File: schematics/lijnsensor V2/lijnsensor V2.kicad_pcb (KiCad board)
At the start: 2 copper layers, 137 x 105 mm, 30 parts, among them J1 Conn_01x04_Pin, U1 USBLC6-2SC6, U10 AS7343xDLG, U11 AS7343xDLG, U2 TCA9548APWR, U3 TLV75718PDBV, U4 AS7343xDLG, U5 AS7343xDLG, U6 AS7343xDLG, U7 AS7343xDLG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

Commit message: update de schematics
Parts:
- added R17: 10K, Resistor_SMD:R_0603_1608Metric, F.Cu at (124.2, 56.4)
- moved C1 3.33 mm to (121.2, 66.8)
- moved C2 2.41 mm to (128.4, 66.1)
- moved U3 1.91 mm to (125.1, 65.8)
- moved U2 1.74 mm to (118.0, 58.4), turned to 180 degrees
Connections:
- U2 pad 3: unconnected-(U2-~{RESET}-Pad3) -> Net-(U2-~{RESET})
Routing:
- net +1V8: track 255.5 -> 0.00 mm
- net Net-(U2-SC3): track 124.9 -> 0.00 mm, vias 8 -> 0
- net Net-(U2-SD3): track 124.5 -> 0.00 mm, vias 6 -> 0
- net Net-(U11-SCL): track 117.5 -> 0.00 mm, vias 4 -> 0
- net Net-(U11-SDA): track 112.7 -> 0.00 mm
- net Net-(U2-SC2): track 92.4 -> 0.00 mm, vias 6 -> 0
- net Net-(U2-SD2): track 91.5 -> 0.00 mm, vias 4 -> 0
- net Net-(U10-SCL): track 87.1 -> 0.00 mm, vias 2 -> 0
- net Net-(U10-SDA): track 82.4 -> 0.00 mm
- net Net-(U2-SD1): track 63.2 -> 0.00 mm
- net Net-(U2-SC1): track 60.0 -> 0.00 mm, vias 4 -> 0
- net Net-(U2-SC5): track 53.8 -> 0.00 mm, vias 2 -> 0
- net Net-(U2-SD5): track 49.4 -> 0.00 mm
- net Net-(U2-SD0): track 22.0 -> 0.00 mm
- net Net-(U2-SC4): track 20.9 -> 0.00 mm
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- removed copper zone on F.Cu, net +3.3V

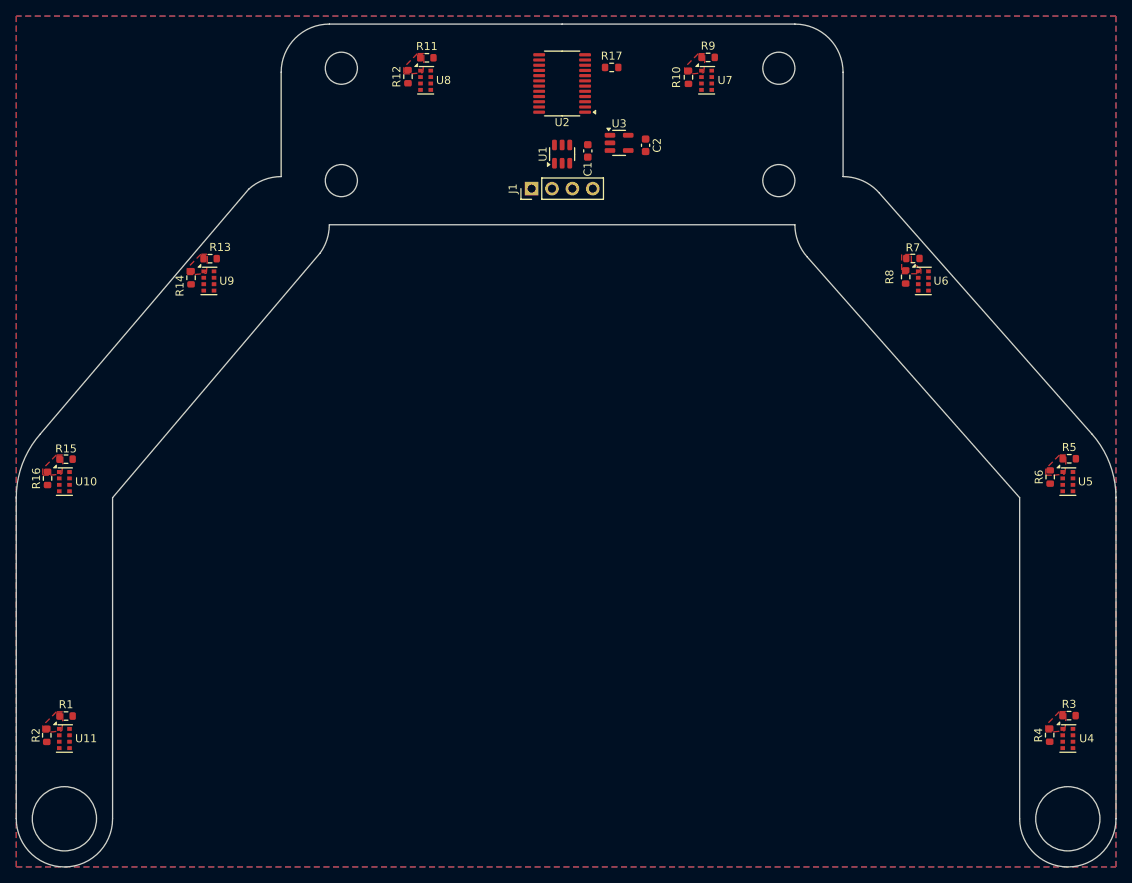
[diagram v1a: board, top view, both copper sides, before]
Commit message: teken al een deel van de lijnsensor
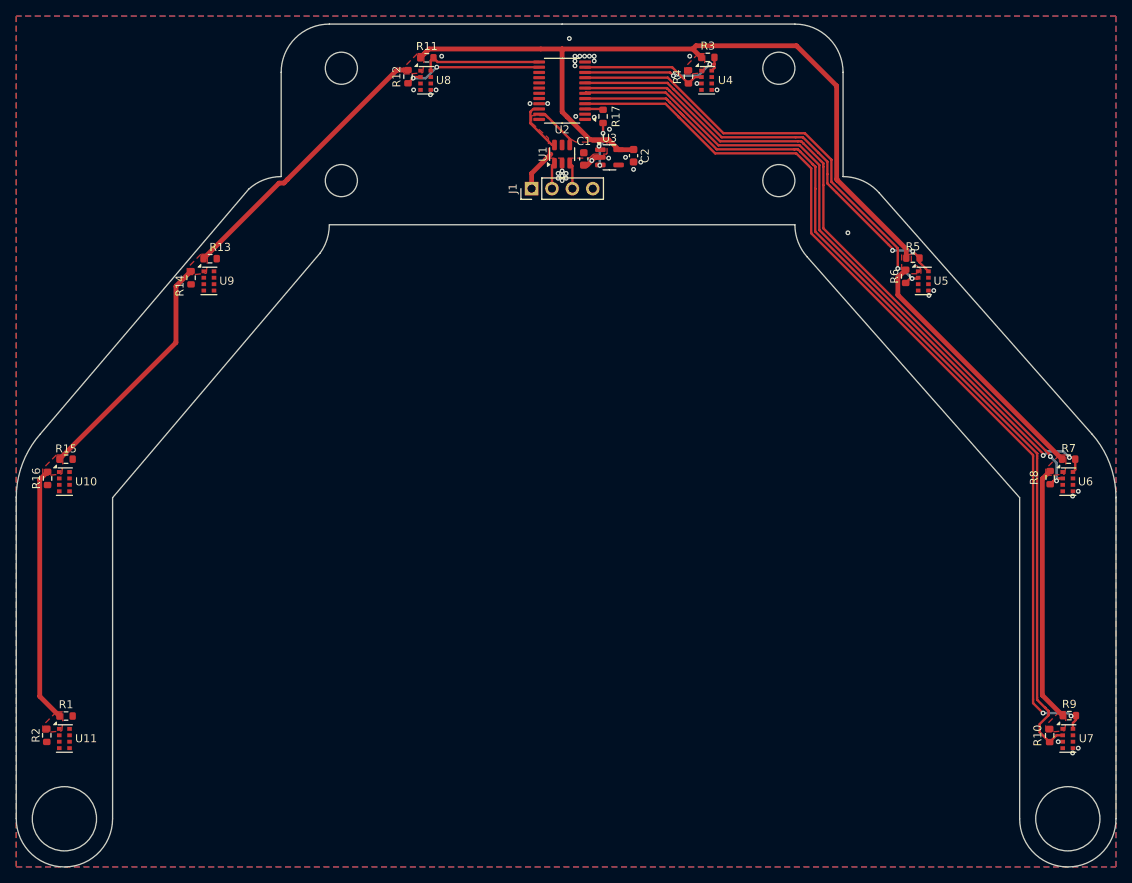
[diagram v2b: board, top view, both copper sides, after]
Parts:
- moved R10 93.5 mm to (178.7, 139.6)
- moved R3 93.5 mm to (136.2, 55.1)
- moved R9 93.5 mm to (181.2, 137.2)
- moved U4 93.5 mm to (136.0, 58.0)
- moved U7 93.5 mm to (181.0, 140.0)
- moved R4 93.5 mm to (133.7, 57.6)
- moved R5 31.7 mm to (161.7, 80.2)
- moved R7 31.6 mm to (181.1, 105.2)
- moved R6 30.8 mm to (160.8, 82.4)
- moved R8 30.8 mm to (178.8, 107.5)
- moved U5 30.8 mm to (163.0, 83.0)
- moved U6 30.8 mm to (181.0, 108.0)
- moved R17 6.19 mm to (123.1, 62.5), turned to 90 degrees
- moved U3 2.16 mm to (123.9, 67.6)
- moved C2 1.98 mm to (126.9, 67.4)
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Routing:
- net +1V8: track 0.00 -> 262.2 mm
- net Net-(U2-SC0): track 0.00 -> 118.9 mm
- net Net-(U2-SD0): track 0.00 -> 117.4 mm, vias 0 -> 2
- net Net-(U2-SD1): track 0.00 -> 87.1 mm, vias 0 -> 2
- net Net-(U2-SC1): track 0.00 -> 87.0 mm, vias 0 -> 2
- net Net-(U2-SC2): track 0.00 -> 56.0 mm, vias 0 -> 2
- net Net-(U2-SD2): track 0.00 -> 54.5 mm, vias 0 -> 2
- net Net-(U2-SD3): track 0.00 -> 18.7 mm, vias 0 -> 2
- net Net-(U2-SC4): track 0.00 -> 18.2 mm, vias 0 -> 2
- net Net-(U2-SC3): track 0.00 -> 15.7 mm
- net Net-(U2-SD4): track 0.00 -> 15.1 mm
- net +3.3V: track 0.00 -> 11.3 mm, vias 0 -> 3
- net /SCL: track 0.00 -> 6.79 mm
- net /SDA: track 0.00 -> 5.84 mm
- net Net-(J1-Pin_3): track 0.00 -> 3.30 mm
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- added copper zone on F.Cu, net +3.3V

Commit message: updata alle afmetingen en maak er een pdf van
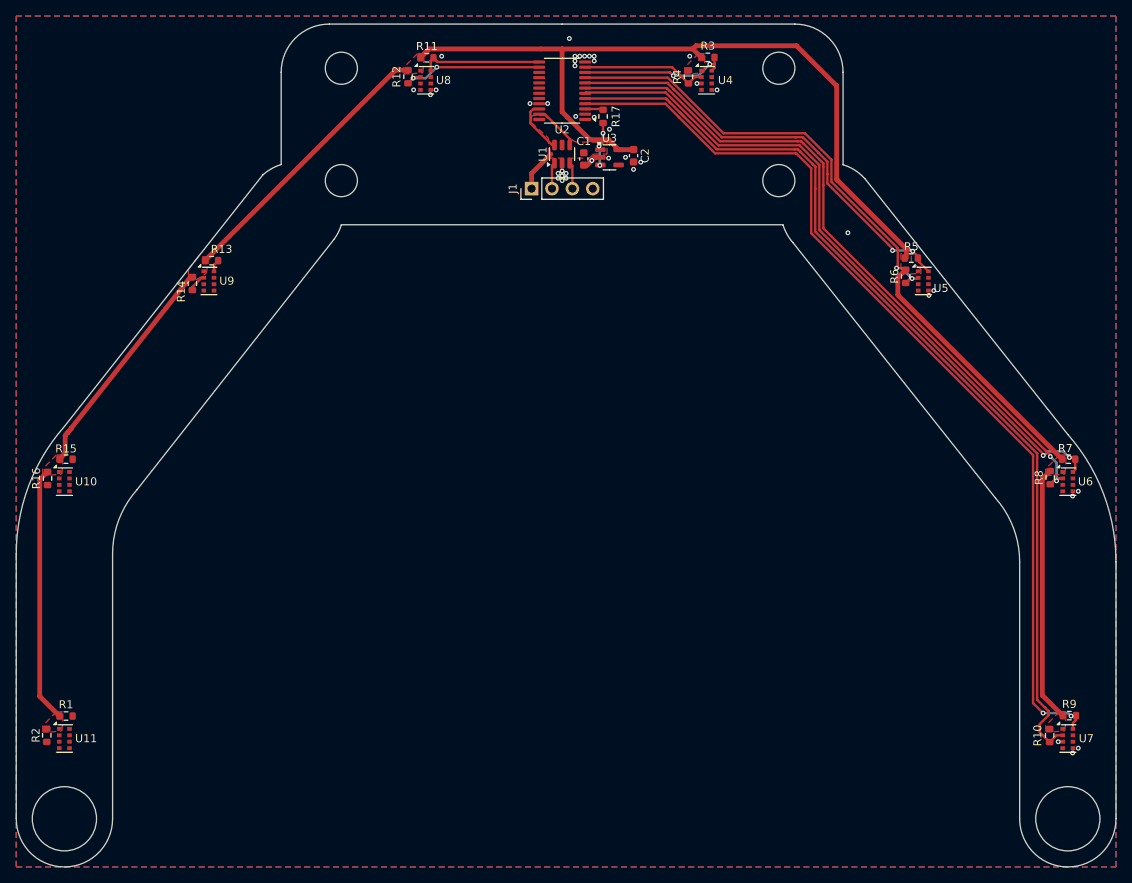
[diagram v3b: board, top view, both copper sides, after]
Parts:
- moved R14 0.74 mm to (71.9, 83.3)
- moved R13 0.30 mm to (74.3, 80.5)
- moved R5 0.20 mm to (161.5, 80.2)
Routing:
- net Net-(U2-SC5): track 0.00 -> 2.29 mm
- net Net-(U2-SC2): track 56.0 -> 58.0 mm
- net +1V8: track 262.2 -> 260.5 mm
- net Net-(U2-SD5): track 0.00 -> 1.54 mm
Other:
- outline, holes or cut-outs redrawn

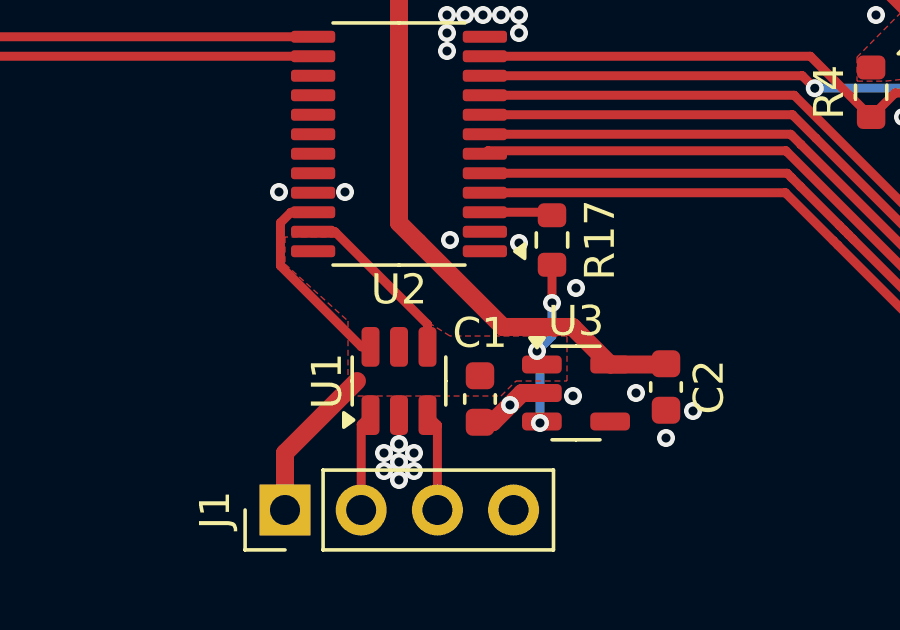
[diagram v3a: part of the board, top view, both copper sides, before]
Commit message: update de .gitignore
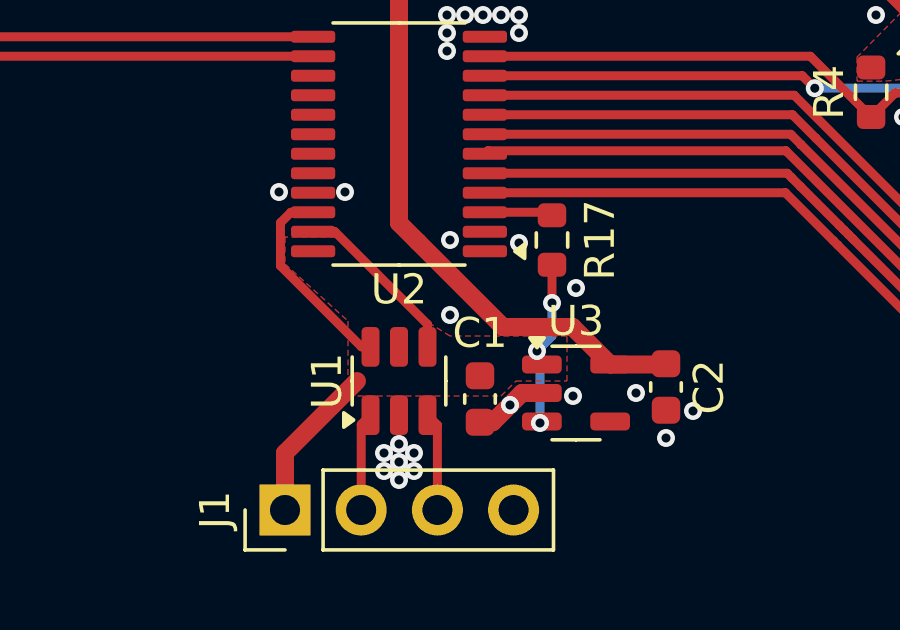
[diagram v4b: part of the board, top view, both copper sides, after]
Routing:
- net GND: vias 41 -> 42
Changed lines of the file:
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@@
+	)
+	(via
+		(at 119.7 65)
+		(size 0.6)
+		(drill 0.3)
+		(layers "F.Cu" "B.Cu")
+		(free yes)
+		(net 5)
 	)
 	(via

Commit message: klaar met lijnsensor V2
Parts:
- moved R13 0.10 mm to (74.4, 80.5)
- moved R5 0.10 mm to (161.4, 80.2)
- moved R14 0.09 mm to (72.0, 83.3)
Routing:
- net Net-(U11-SCL): track 0.00 -> 120.2 mm
- net Net-(U11-SDA): track 0.00 -> 109.3 mm
- net Net-(U10-SCL): track 0.00 -> 86.1 mm, vias 0 -> 2
- net Net-(U10-SDA): track 0.00 -> 82.7 mm
- net Net-(U2-SC5): track 2.29 -> 56.9 mm, vias 0 -> 2
- net Net-(U2-SD5): track 1.54 -> 51.7 mm
- net GND: vias 42 -> 388

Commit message: voeg mijn naam toe aan nieuw hoofd en lijnsensor
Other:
- board text added: "ontworpen door Stan Debakker"
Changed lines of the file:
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@@
 		(layer "User.4")
+	)
+	(gr_text "ontworpen door\nStan Debakker"
+		(at 125.89 64.93 0)
+		(layer "B.SilkS")
+		(effects
+			(font
+				(size 1.5 1.5)
+				(thickness 0.1875)
+			)
+			(justify left bottom mirror)
+		)
 	)
 	(segment

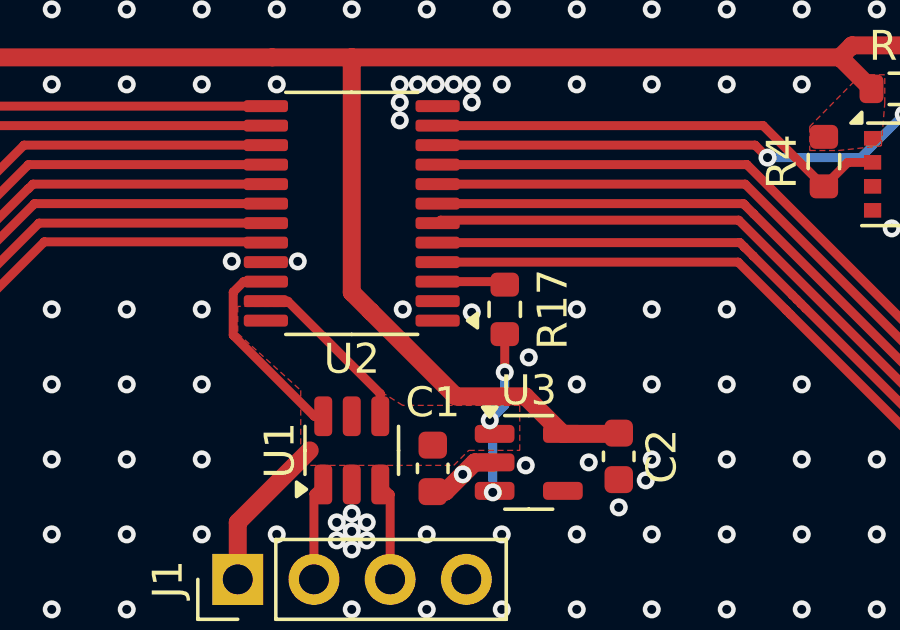
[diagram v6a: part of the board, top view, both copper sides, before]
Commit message: verander het I²C adders van de I²C multiplexer om conflict te vermijden
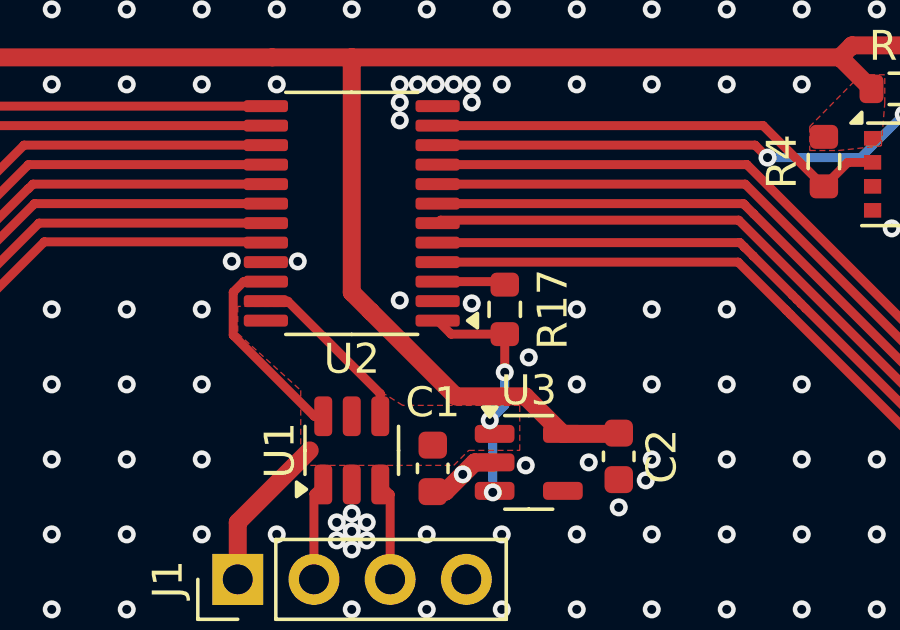
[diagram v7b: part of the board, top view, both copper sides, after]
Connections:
- U2 pad 1: GND -> +3.3V
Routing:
- net +3.3V: track 11.3 -> 13.8 mm
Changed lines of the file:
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@@
 			(layers "F.Cu" "F.Mask" "F.Paste")
 			(roundrect_rratio 0.25)
-			(net 5 "GND")
+			(net 13 "+3.3V")
 			(pinfunction "A0")
 			(pintype "input")
@@
 	)
 	(via
-		(at 122 62.6)
+		(at 122 62.3)
 		(size 0.6)
 		(drill 0.3)
@@
 	)
 	(via
-		(at 119.7 62.5)
+		(at 119.6 62.2)
 		(size 0.6)
 		(drill 0.3)
@@
 		(width 0.3)
 		(layer "F.Cu")
+		(net 13)
+	)
+	(segment
+		(start 123.1 63.325)
+		(end 121.3125 63.325)
+		(width 0.3)
+		(layer "F.Cu")
+		(net 13)
+	)
+	(segment
+		(start 121.3125 63.325)
+		(end 120.8625 62.875)
+		(width 0.3)
+		(layer "F.Cu")

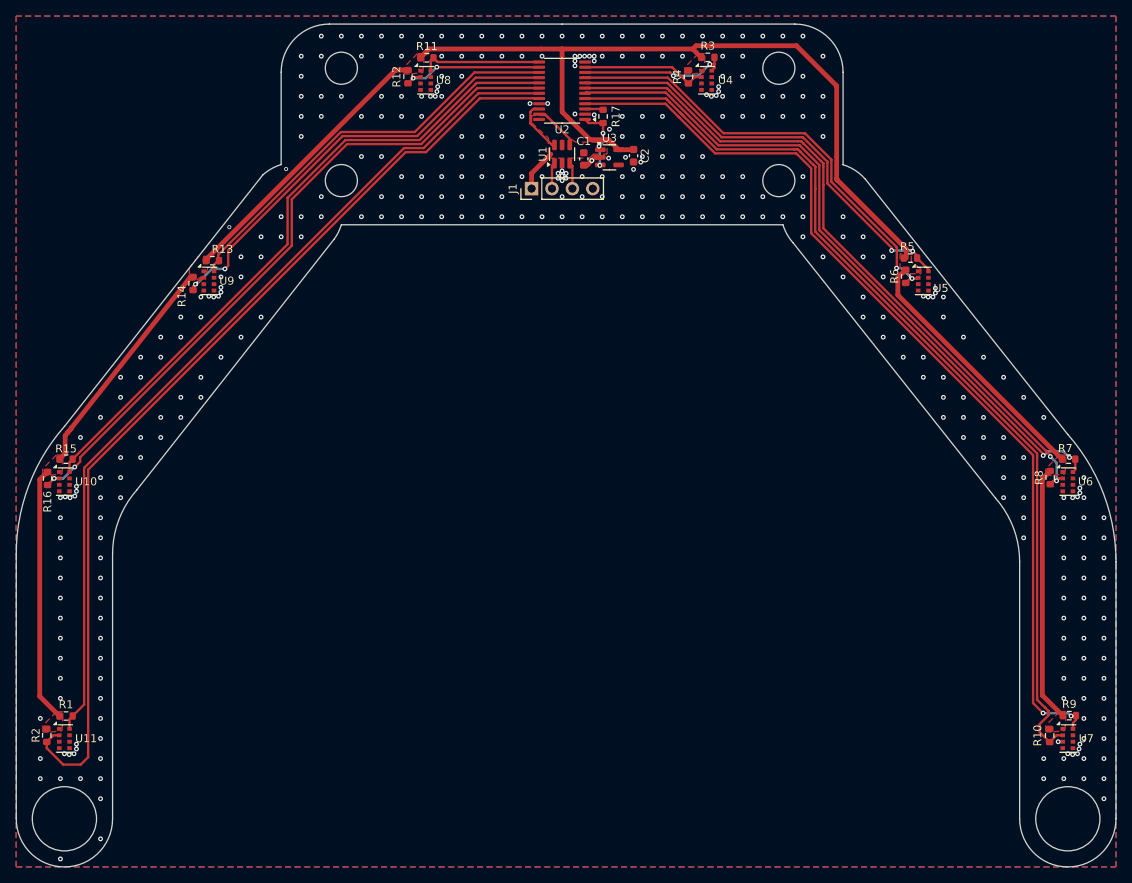
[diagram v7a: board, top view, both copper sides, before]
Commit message: pas de maten aan van de addon V3 en de lijnsensor(nog niet klaar)
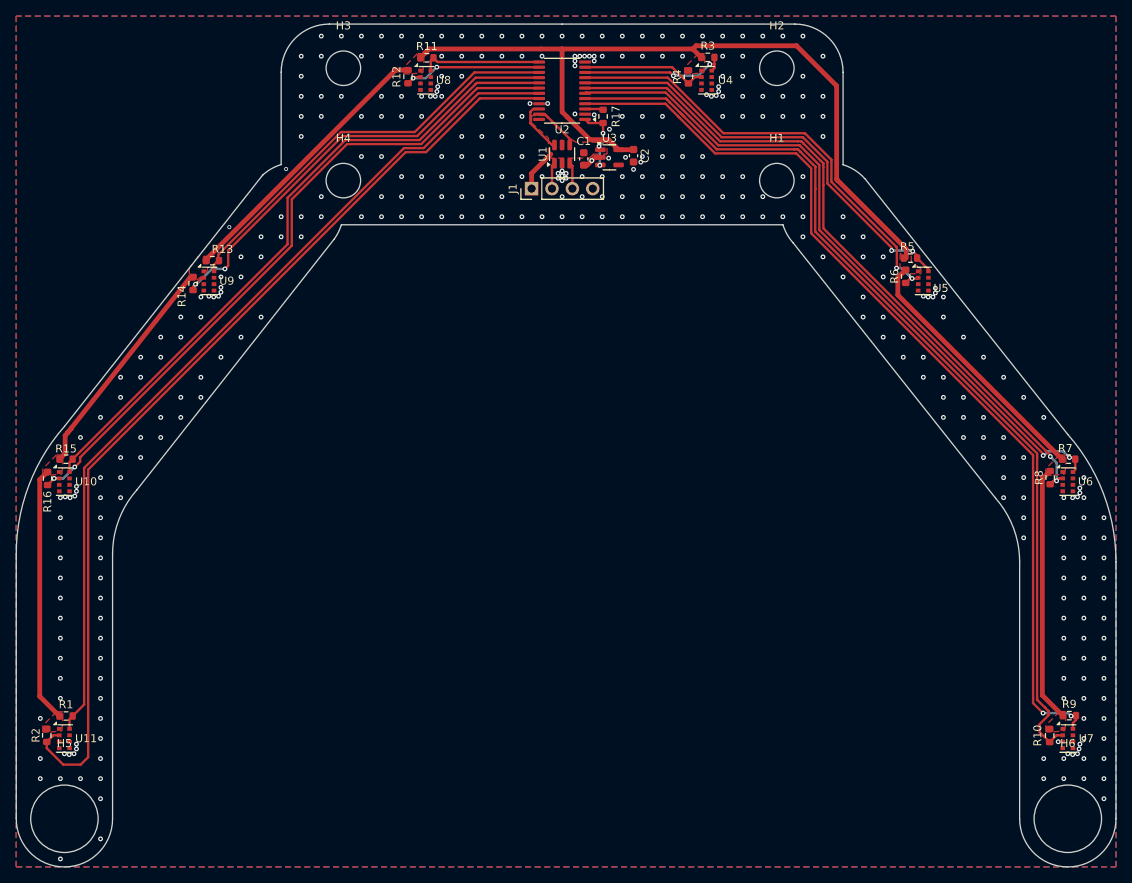
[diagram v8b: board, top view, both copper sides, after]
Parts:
- added H1: MountingHole, MountingHole:MountingHole_4.3mm_M4, F.Cu at (144.8, 70.5)
- added H2: MountingHole, MountingHole:MountingHole_4.3mm_M4, F.Cu at (144.8, 56.5)
- added H3: MountingHole, MountingHole:MountingHole_4.3mm_M4, F.Cu at (90.8, 56.5)
- added H4: MountingHole, MountingHole:MountingHole_4.3mm_M4, F.Cu at (90.8, 70.5)
- added H5: MountingHole, MountingHole:MountingHole_8.4mm_M8, F.Cu at (56.0, 150.0)
- added H6: MountingHole, MountingHole:MountingHole_8.4mm_M8, F.Cu at (181.0, 150.0)
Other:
- outline, holes or cut-outs redrawn
